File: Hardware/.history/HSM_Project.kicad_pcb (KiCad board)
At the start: 2 copper layers, 100.6 x 113.7 mm, 105 parts, among them J1 Conn_01x02_Pin, J10 VL530X Connector, J11 VL530X Connector, J12 VL530X Connector, J13 VL530X Connector, J14 BNO085 Breakout, J16 HC-05 Breakout Board, J2 MP1584 Breakout, J4 TEENSY_4.1, J5 Conn_01x08_Pin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

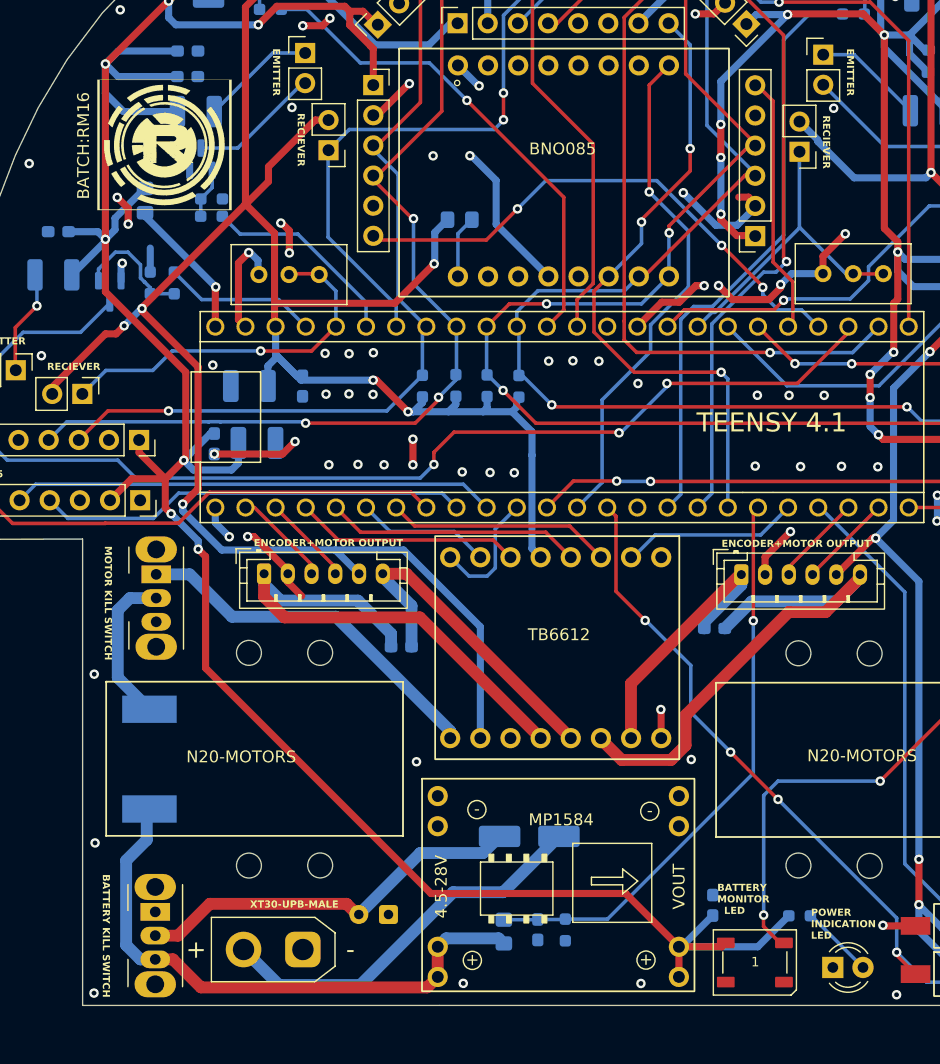
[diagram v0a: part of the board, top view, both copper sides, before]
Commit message: Updated the ootprint of emitter and reciver to pinheader, largened the logo
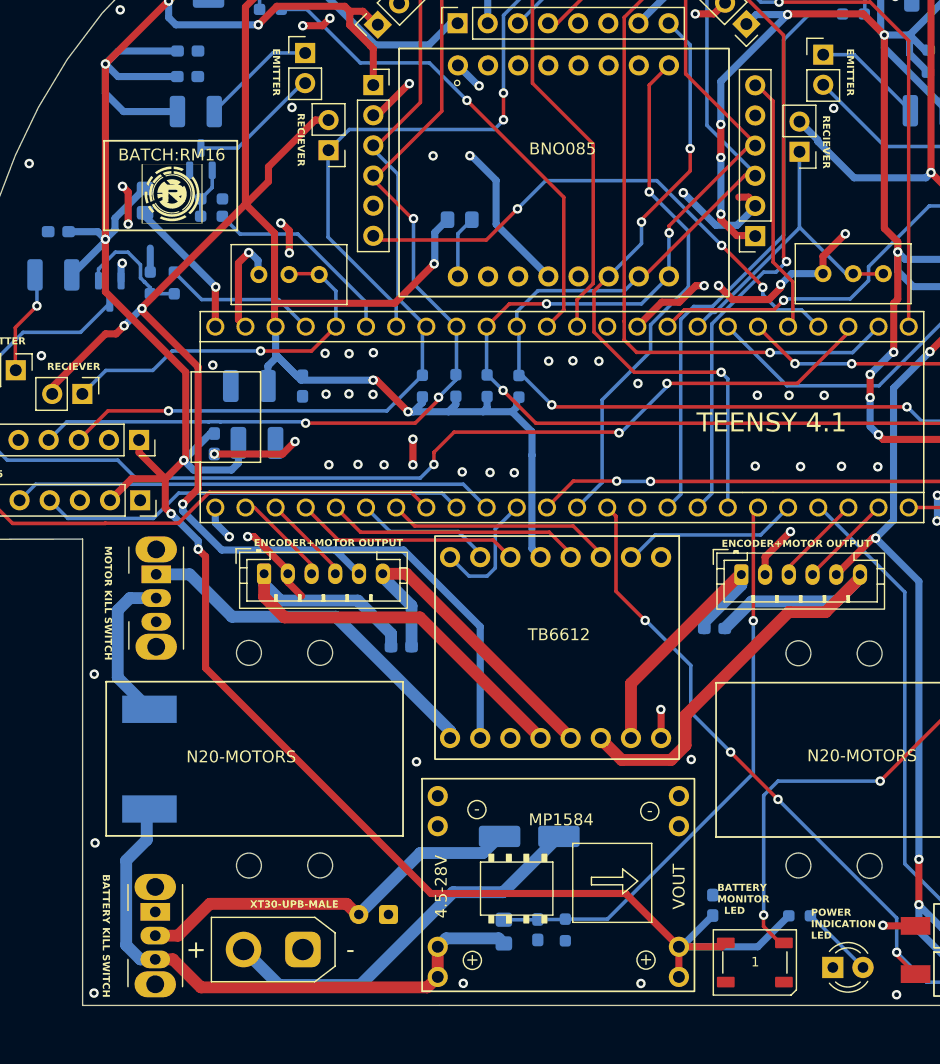
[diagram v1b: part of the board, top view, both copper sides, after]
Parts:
- D3: footprint Micromouse:LED_D3.0mm_micromouse -> LED_THT:LED_D3.0mm
- TB1: value TB6612 Breakout Board -> ~
- moved G*** 4.17 mm to (120.7, 62.9)
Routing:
- net GND: track 140.7 -> 141.4 mm
